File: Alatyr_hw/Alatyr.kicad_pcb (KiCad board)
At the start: 2 copper layers, 30 x 68 mm, 58 parts, among them M1 Vibro_10mm, SW1 IT1198, SW2 IT1198, U1 JDY-23

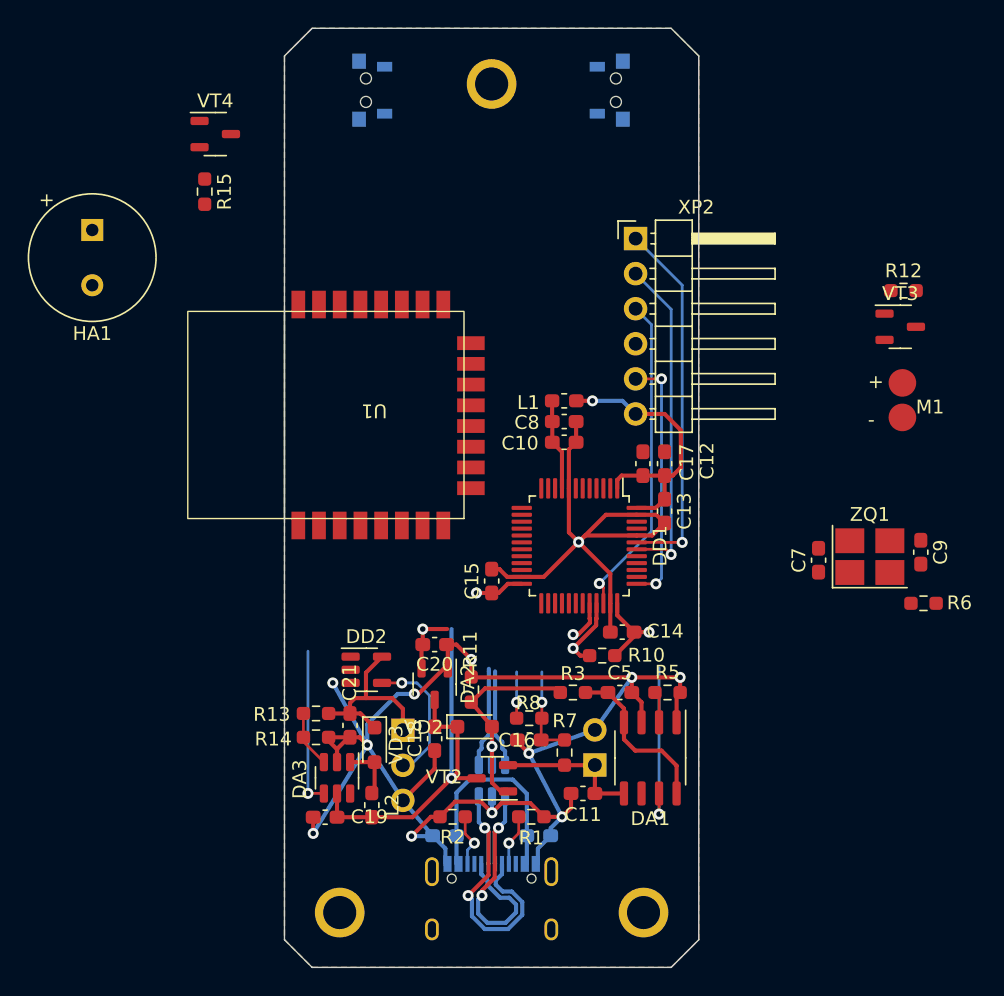
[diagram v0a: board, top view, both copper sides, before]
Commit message: PCB wired, small cover fixes
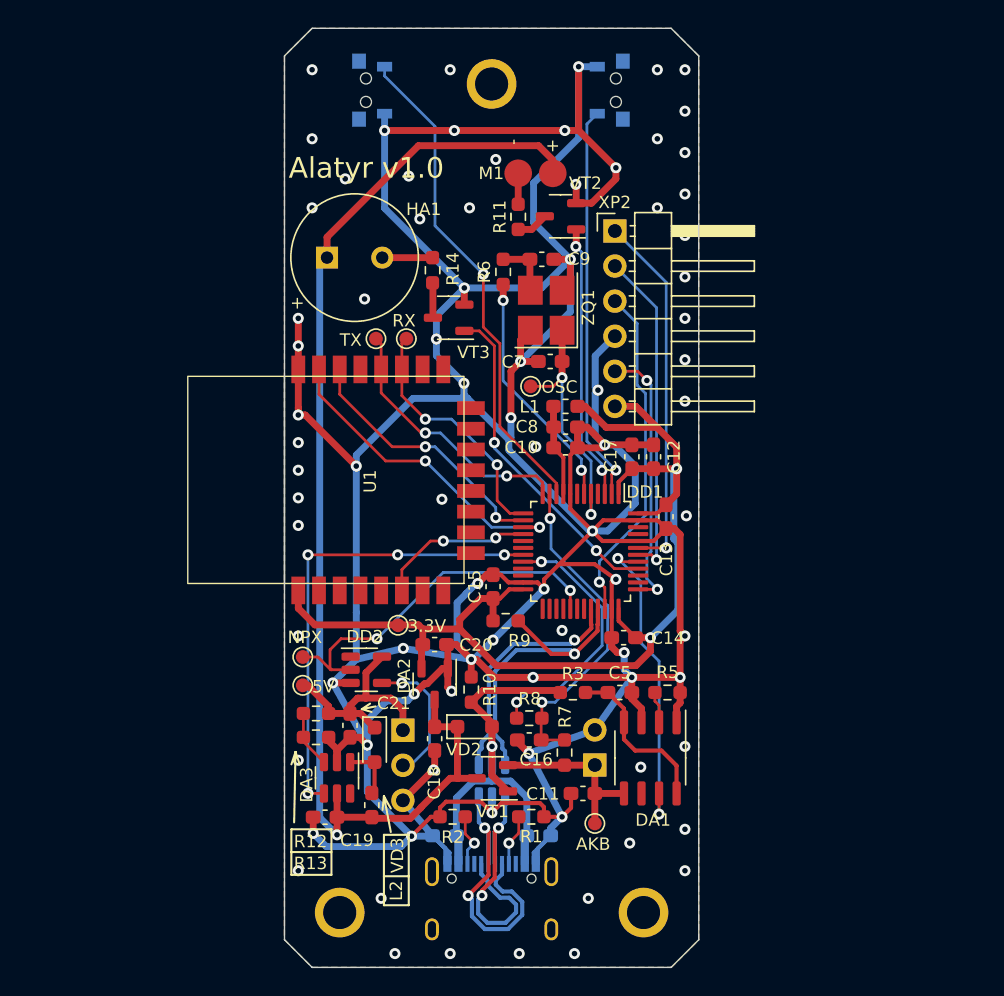
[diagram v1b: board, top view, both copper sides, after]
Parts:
- added TP1: BLE.RX, TestPoint:TestPoint_Pad_D1.0mm, F.Cu at (111.8, 56.5)
- added TP2: BLE.TX, TestPoint:TestPoint_Pad_D1.0mm, F.Cu at (109.6, 56.5)
- added TP3: CLK, TestPoint:TestPoint_Pad_D1.0mm, F.Cu at (120.8, 59.9)
- added TP4: AKB, TestPoint:TestPoint_Pad_D1.0mm, F.Cu at (125.5, 91.6)
- added TP5: NPX, TestPoint:TestPoint_Pad_D1.0mm, F.Cu at (104.3, 79.5)
- added TP6: 3V, TestPoint:TestPoint_Pad_D1.0mm, F.Cu at (111.2, 77.2)
- added TP7: 5V, TestPoint:TestPoint_Pad_D1.0mm, F.Cu at (104.3, 81.6)
- moved R6 38.8 mm to (118.8, 51.6), turned to -90 degrees
- moved C9 34.7 mm to (121.6, 50.7), turned to 0 degrees
- moved M1 31.2 mm to (121.2, 44.5), turned to -90 degrees
- moved ZQ1 29.4 mm to (122.0, 54.4), turned to 90 degrees
- moved R11 28.4 mm to (119.9, 47.6), turned to 90 degrees
- moved VT2 25.9 mm to (123.0, 47.6), turned to 180 degrees
- moved C7 24.2 mm to (122.2, 58.1), turned to 180 degrees
- moved VT3 21.5 mm to (114.9, 55.0), turned to 180 degrees
- moved R14 17.5 mm to (113.7, 51.5), turned to 90 degrees
- moved HA1 17.1 mm to (106.1, 50.6), turned to 90 degrees
- moved R9 7.43 mm to (119.0, 76.9), turned to 180 degrees
- moved U1 4.70 mm to (116.0, 74.2)
- moved XP2 1.60 mm to (126.9, 48.7)
- moved C12 0.94 mm to (129.7, 65.0)
- moved C17 0.94 mm to (128.2, 65.0)
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- renumbered R11 to R10, R12 to R11, R13 to R12, R14 to R13, R15 to R14, R10 to R9, VT2 to VT1, VT3 to VT2, VT4 to VT3
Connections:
- DD1 pad 18: /VIBRO -> unconnected-(DD1-PB0-Pad18)
- DD1 pad 3: unconnected-(DD1-PC14-Pad3) -> /VIBRO
- HA1 pad 1: +3V3 -> /Unst.power
- M1 pad 1: +3V3 -> /Unst.power
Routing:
- net GND: track 148.9 -> 383.2 mm, vias 12 -> 84
- net /Unst.power: track 31.3 -> 86.2 mm
- net +3V3: track 34.9 -> 82.2 mm, vias 4 -> 2
- net /BUT1: track 0.00 -> 36.1 mm, vias 0 -> 1
- net /BUT2: track 0.00 -> 28.8 mm, vias 0 -> 1
- net /NPX.D3V: track 0.00 -> 27.2 mm, vias 0 -> 2
- net /BUZZER: track 0.00 -> 24.1 mm, vias 0 -> 2
- net /BLE.RST: track 0.00 -> 23.0 mm, vias 0 -> 2
- net /5V_EN: track 11.5 -> 34.1 mm, vias 1 -> 4
- net /VIBRO: track 0.00 -> 20.0 mm, vias 0 -> 2
- net /BLE.PWRC: track 0.00 -> 19.3 mm, vias 0 -> 2
- net /BLE.TX: track 0.00 -> 19.3 mm, vias 0 -> 2
- net /OSC_IN: track 0.00 -> 18.2 mm, vias 0 -> 2
- net /BLE.RX: track 0.00 -> 18.1 mm, vias 0 -> 2
- net /OSC_OUT: track 0.00 -> 17.6 mm, vias 0 -> 2
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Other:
- board text added: "3.3V"
- board text added: "5V"
- board text added: "AKB"
- board text added: "AKB+"
- board text added: "AKB-"
- board text added: "Alatyr v1.0"
- board text added: "DIN"
- board text added: "GND"
- board text added: "NPX"
- board text added: "OSC"
- board text added: "RX"
- board text added: "TX"

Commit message: Start writing firmware
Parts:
- H1, H2, H3: footprint Kais_Lib:Hole_2.4 -> MountingHole:MountingHole_2.5mm
- XP1: footprint Connector_PinHeader_2.54mm:PinHeader_1x02_P2.54mm_Horizontal -> Connector_PinHeader_2.54mm:PinHeader_1x02_P2.54mm_Vertical
- XP2: footprint Connector_PinHeader_2.54mm:PinHeader_1x06_P2.54mm_Horizontal -> Connector_PinHeader_2.54mm:PinHeader_1x06_P2.54mm_Vertical
- XP3: footprint Connector_PinHeader_2.54mm:PinHeader_1x03_P2.54mm_Horizontal -> Connector_PinHeader_2.54mm:PinHeader_1x03_P2.54mm_Vertical
- moved TP5 0.90 mm to (105.2, 79.5)
- moved TP7 0.90 mm to (105.2, 81.6)
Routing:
- net GND: track 383.2 -> 399.8 mm, vias 84 -> 81
- net /BUT1: track 36.1 -> 37.2 mm
- net /Unst.power: track 86.2 -> 87.1 mm
- net /NPX.D3V: track 27.2 -> 26.3 mm
- net /NPX.D5V: track 9.99 -> 9.30 mm
- net /5V: track 16.7 -> 16.1 mm
